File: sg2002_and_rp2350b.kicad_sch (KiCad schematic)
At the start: 33 parts, among them CN4 W25Q128FVIQ_Connector, J2 Conn_01x14, J3 Conn_01x14, X3 12MHz

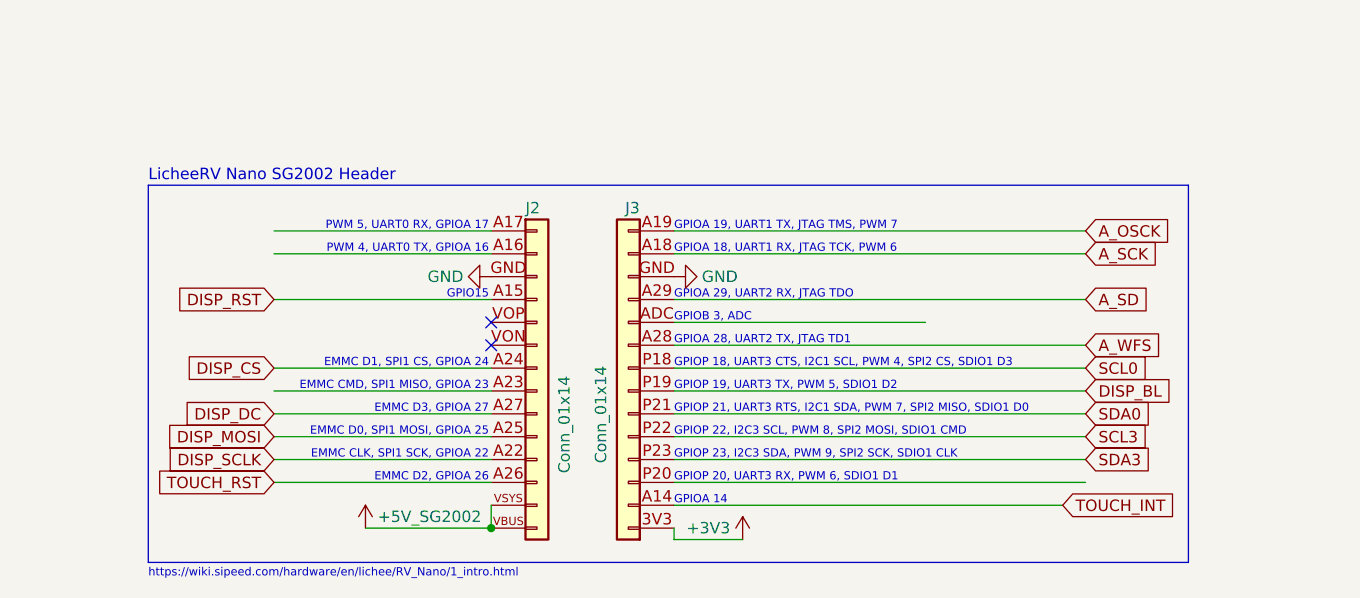
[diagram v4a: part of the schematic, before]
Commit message: Mostly complete initial transfer to hierarchical schematic
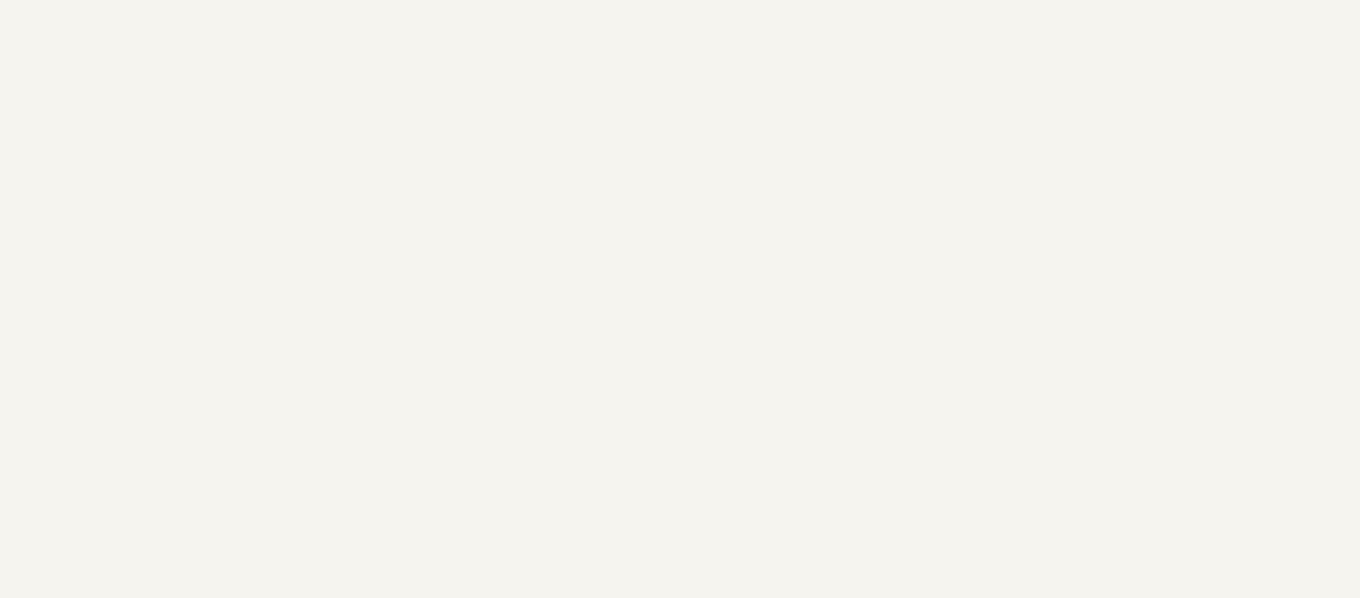
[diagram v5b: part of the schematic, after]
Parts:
- removed J2, J3: Conn_01x14, Connector_PinSocket_2.54mm:PinSocket_1x14_P2.54mm_Vertical, symbol Connector_Generic:Conn_01x14
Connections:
- no-connect marks 24 -> 22
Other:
- note removed: "EMMC CLK, SPI1 SCK, GPIOA 22"
- note removed: "EMMC CMD, SPI1 MISO, GPIOA 23"
- note removed: "EMMC D0, SPI1 MOSI, GPIOA 25"
- note removed: "EMMC D1, SPI1 CS, GPIOA 24"
- note removed: "EMMC D2, GPIOA 26"
- note removed: "EMMC D3, GPIOA 27"
- note removed: "GPIO15"
- note removed: "GPIOA 14"
- note removed: "GPIOA 18, UART1 RX, JTAG TCK, PWM 6"
- note removed: "GPIOA 19, UART1 TX, JTAG TMS, PWM 7"
- note removed: "GPIOA 28, UART2 TX, JTAG TD1"
- note removed: "GPIOA 29, UART2 RX, JTAG TDO"
- note removed: "GPIOB 3, ADC"
- note removed: "GPIOP 18, UART3 CTS, I2C1 SCL, PWM 4, SPI2 CS, SDIO1 D3"
- note removed: "GPIOP 19, UART3 TX, PWM 5, SDIO1 D2"
- note removed: "GPIOP 20, UART3 RX, PWM 6, SDIO1 D1"
- note removed: "GPIOP 21, UART3 RTS, I2C1 SDA, PWM 7, SPI2 MISO, SDIO1 D0"
- note removed: "GPIOP 22, I2C3 SCL, PWM 8, SPI2 MOSI, SDIO1 CMD"
- note removed: "GPIOP 23, I2C3 SDA, PWM 9, SPI2 SCK, SDIO1 CLK"
- note removed: "LicheeRV Nano SG2002 Header"
- note removed: "PWM 4, UART0 TX, GPIOA 16"
- note removed: "PWM 5, UART0 RX, GPIOA 17"
- note removed: "https://wiki.sipeed.com/hardware/en/lichee/RV_Nano/1_intro.html"

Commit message: Transferred everything to hierarchical schematic and wired PSU power on circuit AND created duplicate schematics for all relevant subsystems
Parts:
- removed BOOTSEL1, RESET1: TS-1088-AR02016, JLCImport:TS-1088-AR02016, symbol JLCImport:TS-1088-AR02016
- removed C50, C51, C54: 4.7uF, Capacitor_SMD:C_0402_1005Metric, symbol JLCImport:CL05A475MP5NRNC
- removed C52, C53, C55, C56, C57, C58, C59, C60, C61, C62, C63, C64: 100nF, Capacitor_SMD:C_0402_1005Metric, symbol JLCImport:CL05B104KB54PNC
- removed C65, C66: 33pF, Capacitor_SMD:C_0402_1005Metric, symbol JLCImport:0402CG330J500NT
- removed CN4: W25Q128FVIQ_Connector, JLCImport:H2541FV-C762-2X04P, symbol JLCImport:H2541FV-C762-2X04P
- removed L4: 3.3uH, JLCImport:AOTA-B201610S3R3-101-T, symbol JLCImport:AOTA-B201610S3R3-101-T
- removed PI0: RP2350B, JLCImport:RP2350B_C42415655, symbol MCU_RaspberryPi:RP2350B
- removed PI0_Debug1: Conn_01x03, Connector_PinHeader_2.54mm:PinHeader_1x03_P2.54mm_Vertical, symbol Connector_Generic:Conn_01x03
- removed R44: 33, Resistor_SMD:R_0402_1005Metric, symbol JLCImport:0402WGF330JTCE
- removed R45, R46: 27, Resistor_SMD:R_0603_1608Metric, symbol JLCImport:0603WAF270JT5E
- removed R47, R48: 1k, Resistor_SMD:R_0402_1005Metric, symbol JLCImport:0402WGF1001TCE
- removed R49: 220, Resistor_SMD:R_0603_1608Metric, symbol JLCImport:0603WAF2200T5E
- removed USB_PI0: MICRO_180_ZB, JLCImport:MICRO_180_ZB, symbol JLCImport:MICRO_180_ZB
- removed X3: 12MHz, JLCImport:X322512MSB4SI, symbol JLCImport:X322512MSB4SI
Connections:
- no-connect marks 22 -> 0
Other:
- note removed: "Additional SATA GPIO pins spread across other RP2350B's for easier routing"
- note removed: "Debug pins, solder by hand to save $$"
- note removed: "Dual 33pF capacitors is to achieve 16.5pF + ~3pF (parasitic) = ~19.5pF total, but 220ohm res is eyeballed, needs testing"
- note removed: "Ensure USB_DM and USB_DP resistors are as close to RP2350B as possible"
- note removed: "I2C, to SG2002"
- note removed: "PWM, to fans"
- note removed: "Reset Button"
- note removed: "SATA Current Monitoring"
- note removed: "SATA0"
- note removed: "SATA1"
- note removed: "SATA2"
- note removed: "SATA3"
- note removed: "SATA4"
- note removed: "SATA5"
- note removed: "TODO: verify how the PWM works on the RP2350"
- note removed: "There's a lot of extra resistors on CS# in the example design, but they label them as DNF, so I've excluded them."
- note removed: "USB Boot Button Default -> Flash boot"
- note removed: "VBUS left floating bc Pi can get VCC from the PSU"
